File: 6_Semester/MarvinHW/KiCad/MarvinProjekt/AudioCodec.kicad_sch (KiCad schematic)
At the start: 0 parts

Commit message: made SD-Card, Audio Codec and Amplifier schematic
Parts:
- added C10, C11, C12, C13, C14, C15, C16, C17, C18, C19, C20, C21, C22, C23, C24, C25, C26, C27, C28, C29, C30, C31, C32, C5, C6, C7, C8, C9: C, symbol Device:C
- added FB1: Ferrite_Bead_Small, Inductor_SMD:L_0805_2012Metric, symbol Device:FerriteBead_Small
- added LS1: Speaker, symbol Device:Speaker
- added R10, R11, R12, R13, R14, R15, R16, R17, R18, R19, R20, R21, R22, R23, R24, R25, R26, R4, R5, R6, R7, R8, R9: R, symbol Device:R
- added U2: ~, Package_DFN_QFN:QFN-28-1EP_4x4mm_P0.4mm_EP2.3x2.3mm, symbol Library:ES8388
- added U3: ~, symbol Library:NS4150
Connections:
- new net: R22.2, R24.1, U3.2 (INP)
- new net: R14.1, U2.7
- new net: C23.1, C24.1, C25.1, FB1.2, U3.1 (VIN), U3.10 (PVIN)
- new net: R12.1, U2.1
- new net: C15.1, C18.1, U2.10
- new net: C20.2, U2.11
- new net: C19.2, U2.12
- new net: C7.1, C9.1, R6.2, U2.17
- new net: C14.1, C17.1, U2.19
- new net: C5.1, R4.1, R5.1, U2.2, U2.3
- new net: C13.1, C16.1, U2.20
- new net: C11.1, R9.1, U2.27
- new net: C12.1, R8.1, U2.28
- new net: R13.1, U2.5
- new net: R15.1, U2.6
- new net: R16.1, U2.8
- new net: C30.1, C32.1, LS1.1, R25.1
- new net: C28.1, C29.1
- new net: C19.1, R19.2
- new net: C26.1, C27.2, R22.1
- new net: C22.1, R21.1
- new net: C20.1, R20.2
- new net: R23.2, U3.3 (INN)
- new net: C31.2, C32.2, LS1.2, R26.1
- new net: C28.2, R23.1
- new net +3V3: C10.1, C6.1, C8.1, FB1.1, R10.1, R11.1, R17.1, R5.2, R6.1, R7.1, R7.2, U2.16
- new net ASDOUT: R16.2
- new net AUDIO_LS: C27.1, R21.2
- new net AUDIO_RL: C21.1, C22.2
- new net Audio_RL: R19.1, R20.1
- new net CE: R17.2, R18.1, U2.26
- new net DSDIN: R15.2
- new net GND: C10.2, C11.2, C12.2, C13.2, C14.2, C15.2, C16.2, C17.2, C18.2, C21.2, C23.2, C24.2, C25.2, C26.2, C29.2, C30.2, C31.1, C5.2, C6.2, C7.2, C8.2, C9.2, R18.2, R24.2, R4.2, U2.13, U2.18, U2.29, U2.4, U3.11 (GNDPAD), U3.4 (DGND), U3.6 (CLK), U3.7 (PGND)
- new net LRCK: R14.2
- new net LS+: R25.2, U3.8 (OUTP)
- new net LS-: R26.2, U3.9 (OUTN)
- new net LS_ENABLE: U3.5 (!SHDN)
- new net MCLK: R12.2
- new net SCL: R10.2, R8.2
- new net SCLK: R13.2
- new net SDA: R11.2, R9.2
- no-connect marks 0 -> 8
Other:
- note added: "AudioCodec schaltung Verstärker schaltung"
- note added: "Components near IC pins on the same layer, NO VIAS!"

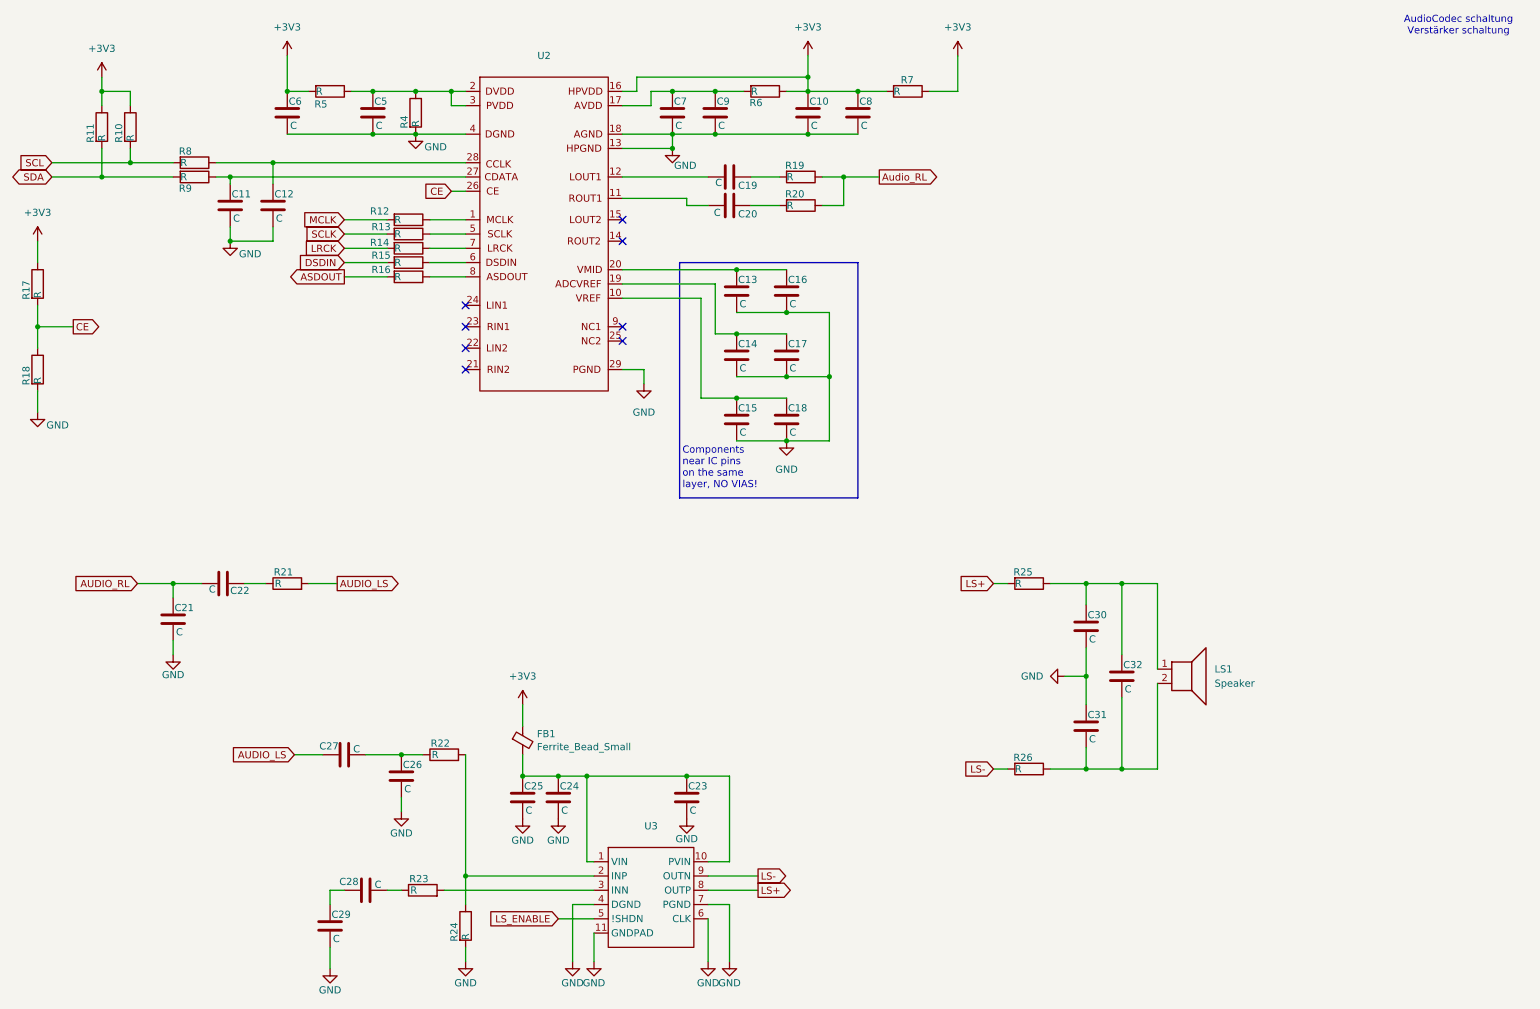
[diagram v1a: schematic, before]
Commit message: added datasheets and worked on schematic
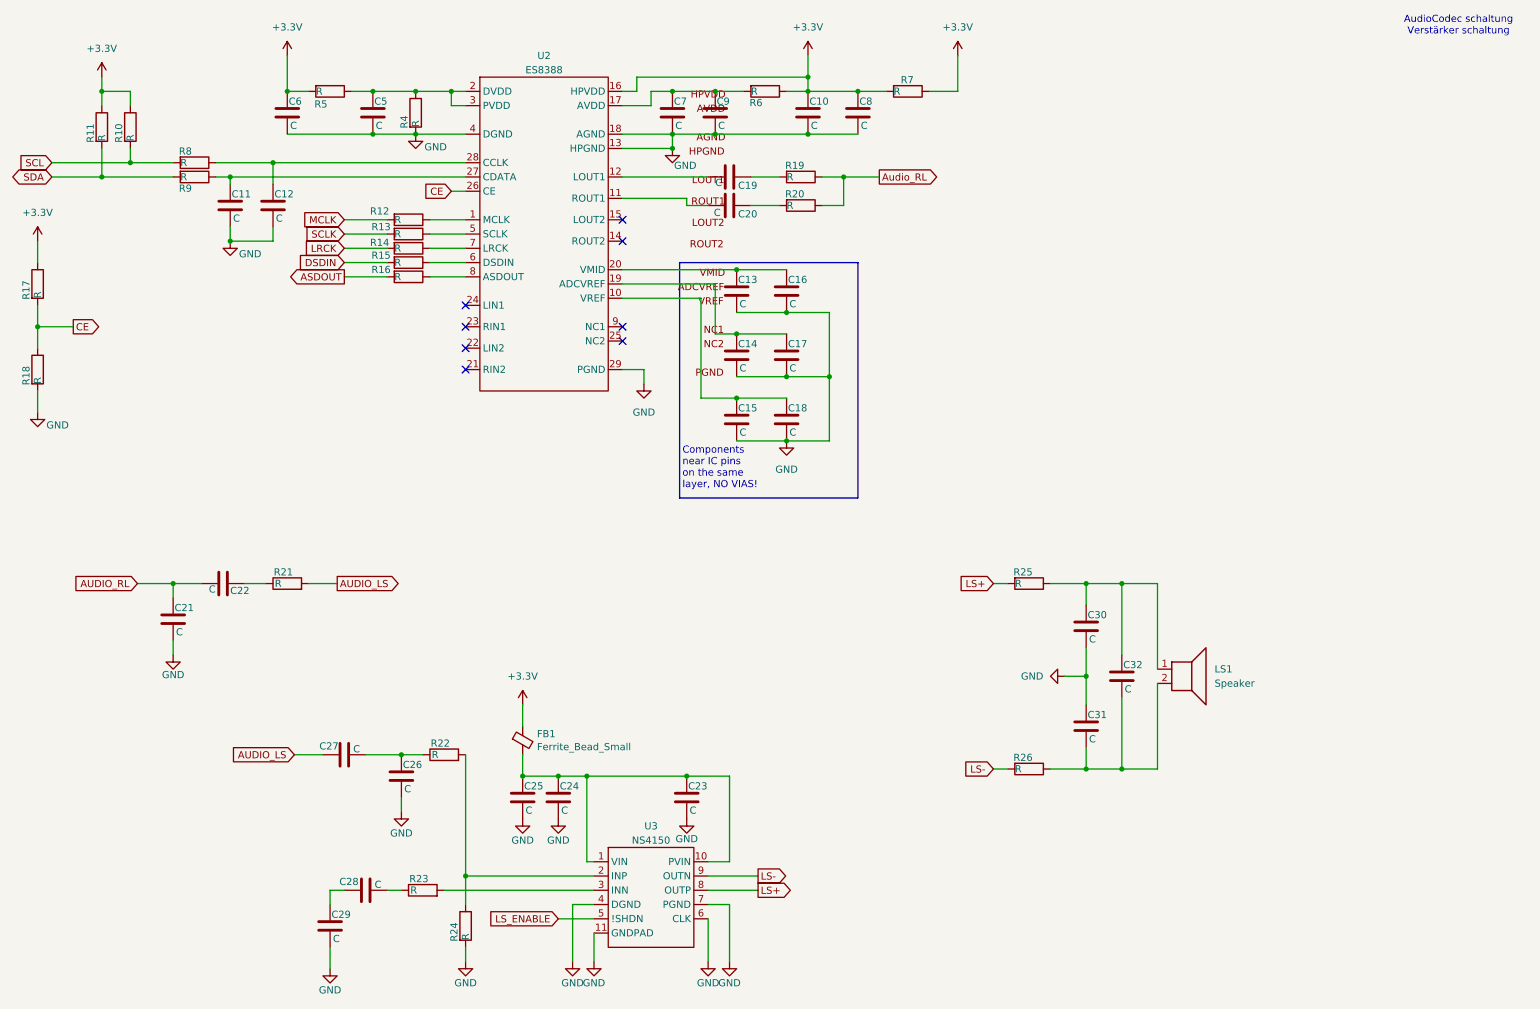
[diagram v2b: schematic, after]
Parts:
- U2: value ~ -> ES8388
- U3: value ~ -> NS4150
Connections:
- net +3V3 renamed +3.3V

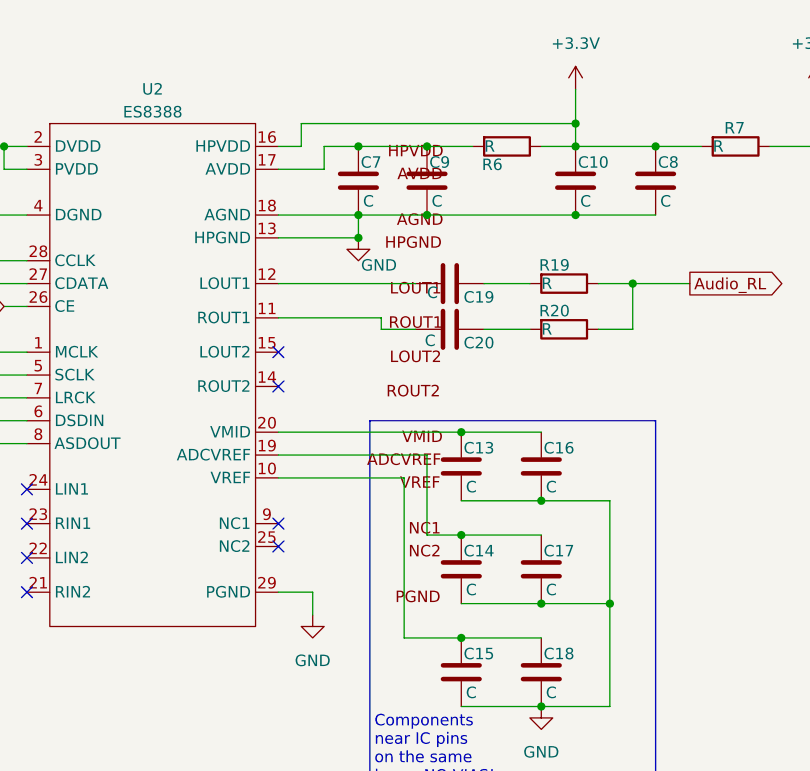
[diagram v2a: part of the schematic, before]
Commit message: renamed untitledsheet to crontrol
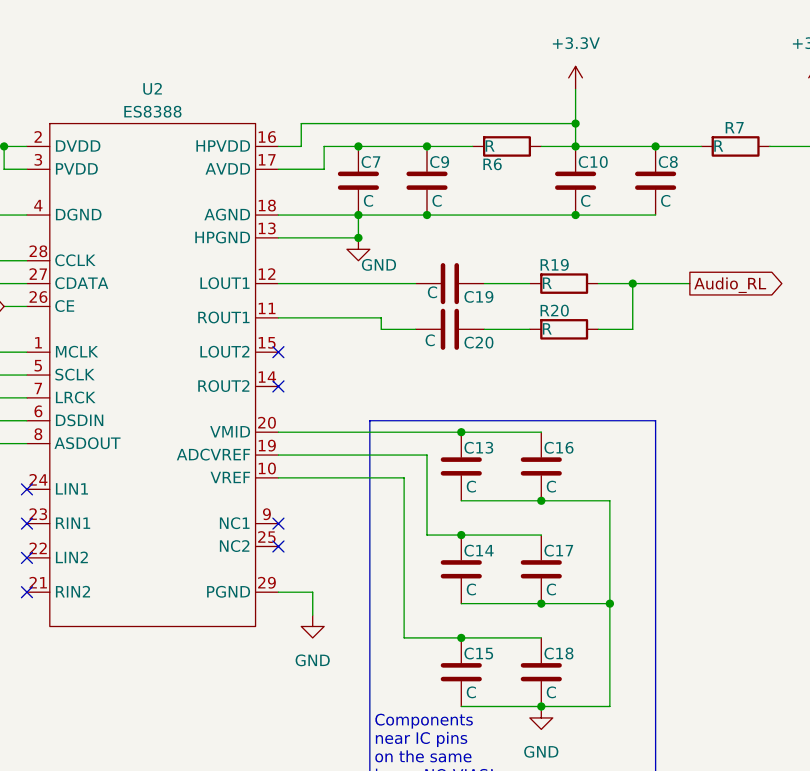
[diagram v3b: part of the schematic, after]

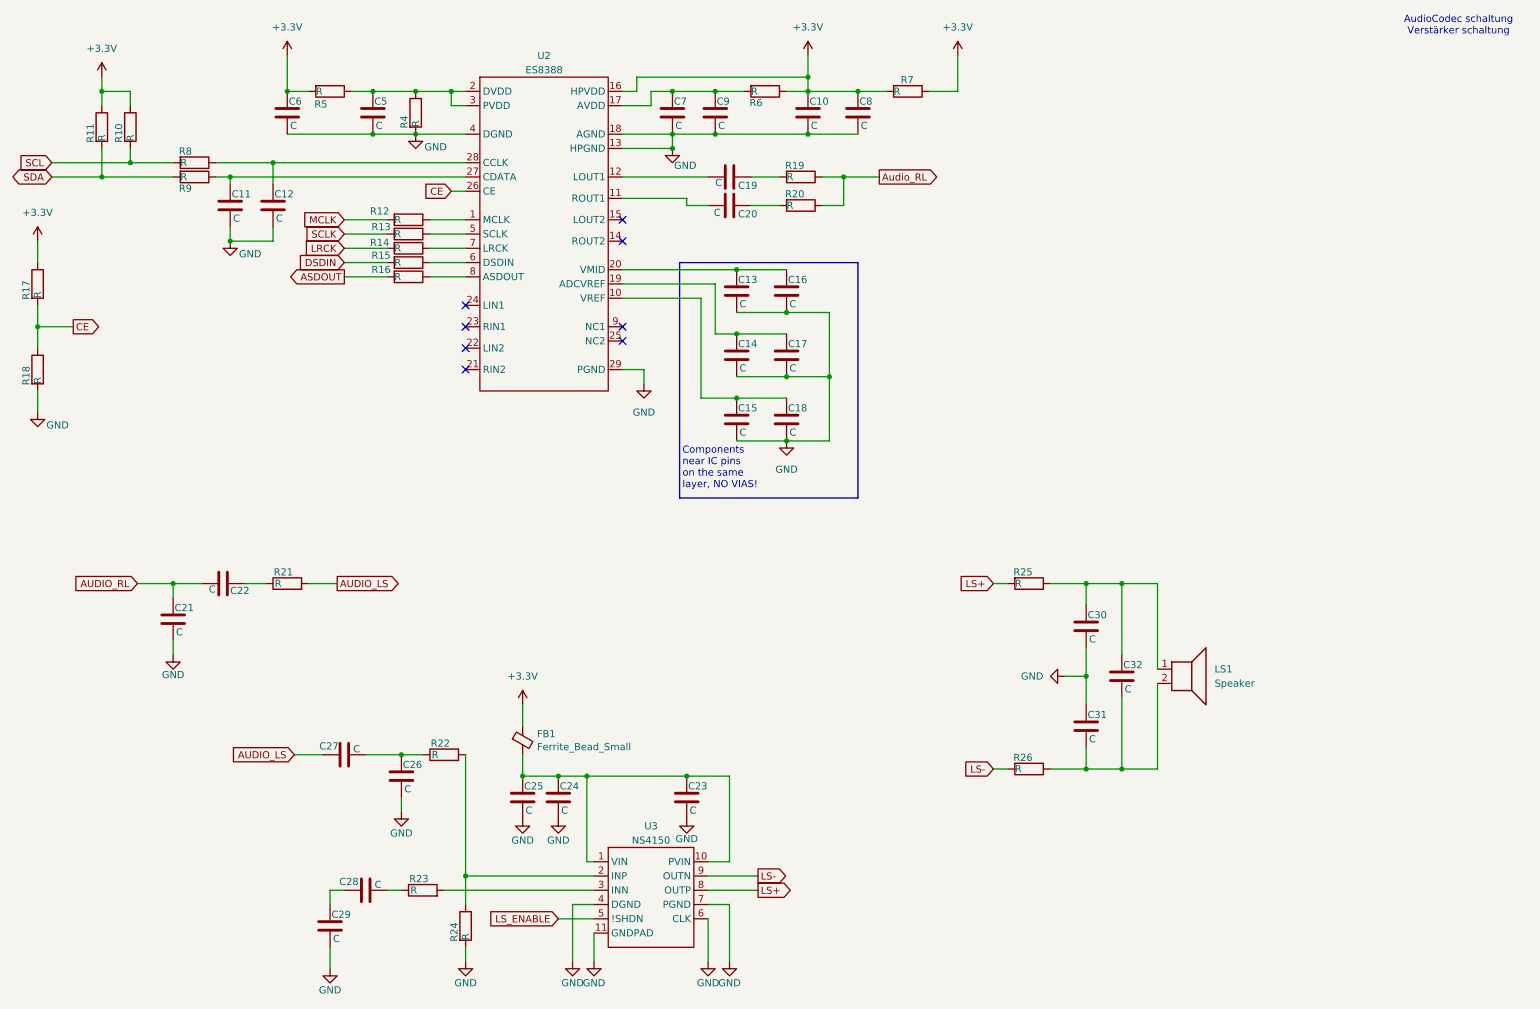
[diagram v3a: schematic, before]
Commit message: finished schematic working on footprints
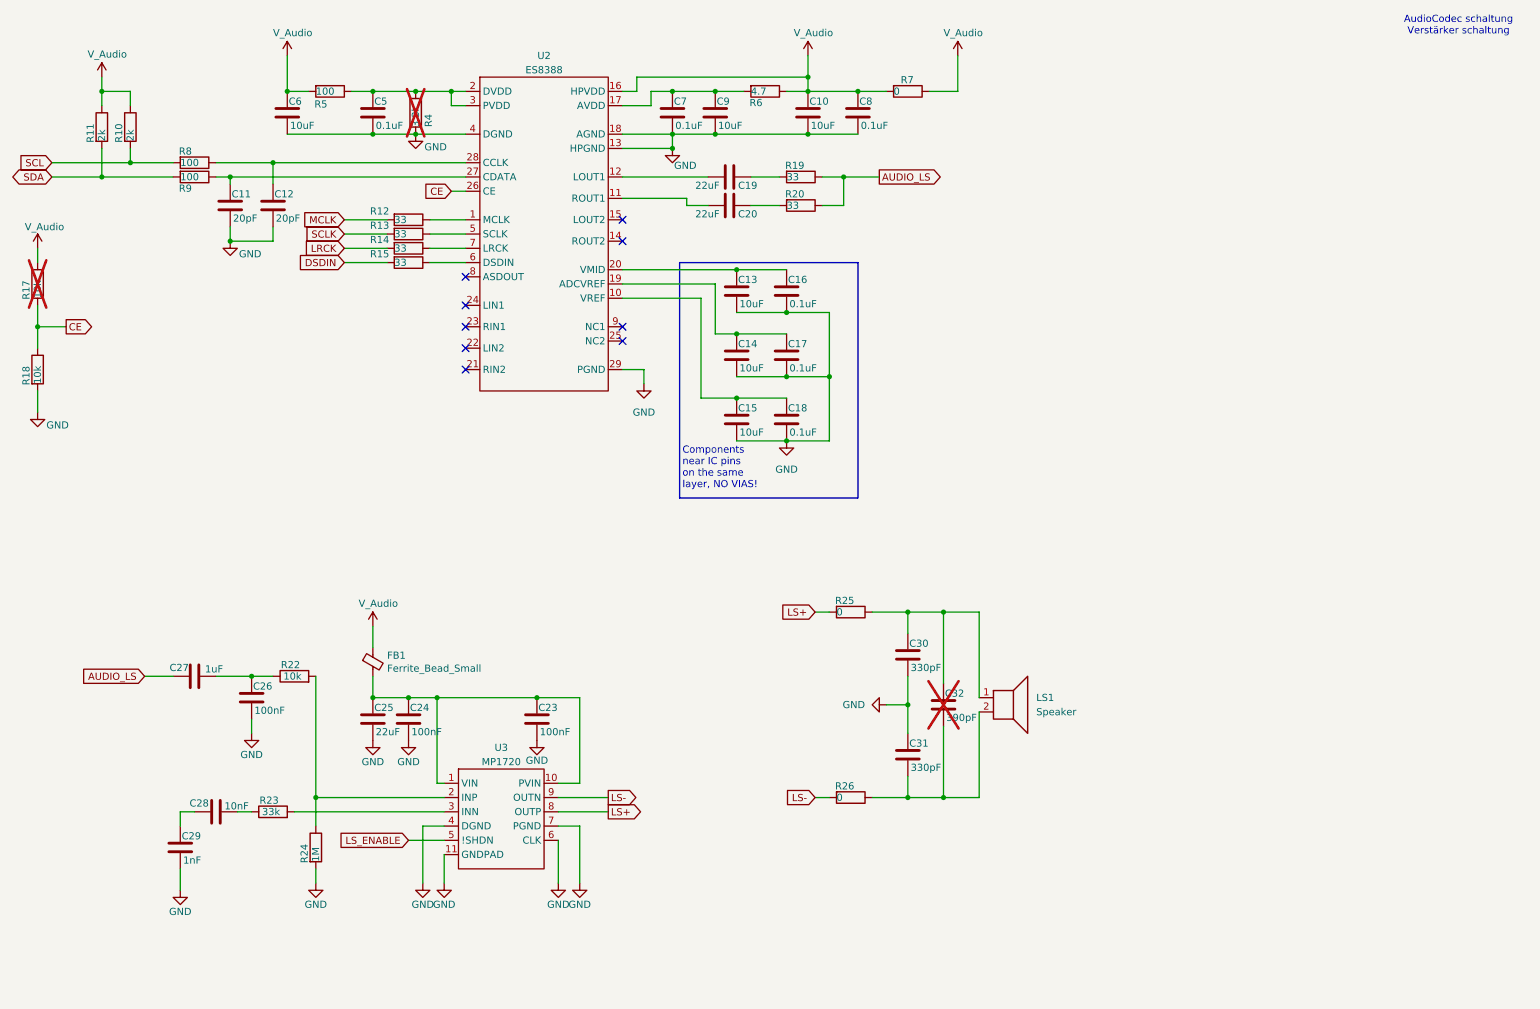
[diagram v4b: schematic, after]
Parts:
- removed C21, C22: C, symbol Device:C
- removed R16, R21: R, symbol Device:R
- C10, C13, C14, C15, C6, C9: value C -> 10uF; footprint (none) -> Capacitor_SMD:C_1206_3216Metric_Pad1.33x1.80mm_HandSolder
- C11, C12: value C -> 20pF; footprint (none) -> Capacitor_SMD:C_0805_2012Metric_Pad1.18x1.45mm_HandSolder
- C16, C17, C18, C5, C7, C8: value C -> 0.1uF; footprint (none) -> Capacitor_SMD:C_0805_2012Metric_Pad1.18x1.45mm_HandSolder
- C19, C20, C25: value C -> 22uF; footprint (none) -> Capacitor_SMD:C_0805_2012Metric_Pad1.18x1.45mm_HandSolder
- C23, C24, C26: value C -> 100nF; footprint (none) -> Capacitor_SMD:C_0805_2012Metric_Pad1.18x1.45mm_HandSolder
- C27: value C -> 1uF; footprint (none) -> Capacitor_SMD:C_0805_2012Metric_Pad1.18x1.45mm_HandSolder
- C28: value C -> 10nF; footprint (none) -> Capacitor_SMD:C_0805_2012Metric_Pad1.18x1.45mm_HandSolder
- C29: value C -> 1nF; footprint (none) -> Capacitor_SMD:C_0805_2012Metric_Pad1.18x1.45mm_HandSolder
- C30, C31: value C -> 330pF; footprint (none) -> Capacitor_SMD:C_0805_2012Metric_Pad1.18x1.45mm_HandSolder
- C32: value C -> 390pF; footprint (none) -> Capacitor_SMD:C_0805_2012Metric_Pad1.18x1.45mm_HandSolder; now not fitted
- R10, R11: value R -> 2k; footprint (none) -> Resistor_SMD:R_0805_2012Metric_Pad1.20x1.40mm_HandSolder
- R12, R13, R14, R15, R19, R20: value R -> 33; footprint (none) -> Resistor_SMD:R_0805_2012Metric_Pad1.20x1.40mm_HandSolder
- R17: value R -> 10k; footprint (none) -> Resistor_SMD:R_0805_2012Metric_Pad1.20x1.40mm_HandSolder; now not fitted
- R18, R22: value R -> 10k; footprint (none) -> Resistor_SMD:R_0805_2012Metric_Pad1.20x1.40mm_HandSolder
- R23: value R -> 33k; footprint (none) -> Resistor_SMD:R_0805_2012Metric_Pad1.20x1.40mm_HandSolder
- R24: value R -> 1M; footprint (none) -> Resistor_SMD:R_0805_2012Metric_Pad1.20x1.40mm_HandSolder
- R25, R26, R7: value R -> 0; footprint (none) -> Resistor_SMD:R_0805_2012Metric_Pad1.20x1.40mm_HandSolder
- R4: value R -> 3.3k; footprint (none) -> Resistor_SMD:R_0805_2012Metric_Pad1.20x1.40mm_HandSolder; now not fitted
- R5, R8, R9: value R -> 100; footprint (none) -> Resistor_SMD:R_0805_2012Metric_Pad1.20x1.40mm_HandSolder
- R6: value R -> 4.7; footprint (none) -> Resistor_SMD:R_0805_2012Metric_Pad1.20x1.40mm_HandSolder
- U3: value NS4150 -> MP1720
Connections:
- net Audio_RL is gone; now on net AUDIO_LS: R19.1, R20.1
- net +3.3V renamed V_Audio
- no-connect marks 8 -> 9
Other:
- moved on the sheet: C23, C24, C25, C26, C27, C28, C29, C30, C31, FB1, LS1, R22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

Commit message: finished all footprints and put the objects in place
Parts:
- LS1: footprint (none) -> Library:LS
- U3: footprint (none) -> Library:MP1720
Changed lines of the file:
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@@
 			)
 		)
-		(property "Footprint" ""
+		(property "Footprint" "Library:MP1720"
 			(at 102.87 153.67 0)
 			(effects
@@
 			)
 		)
-		(property "Footprint" ""
+		(property "Footprint" "Library:LS"
 			(at 193.04 139.7 0)
 			(effects

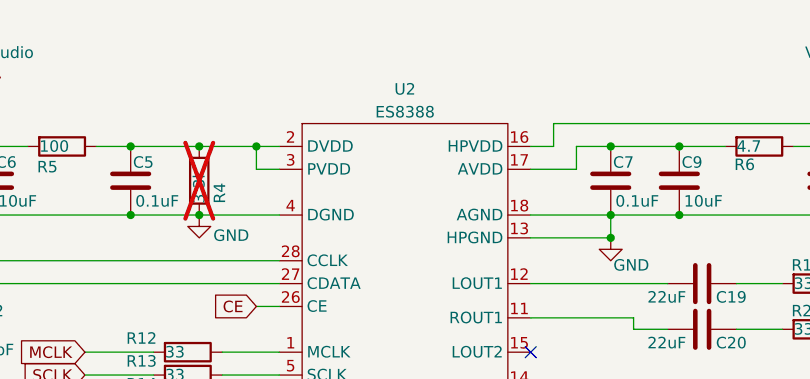
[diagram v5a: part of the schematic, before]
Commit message: add comonents to BoM
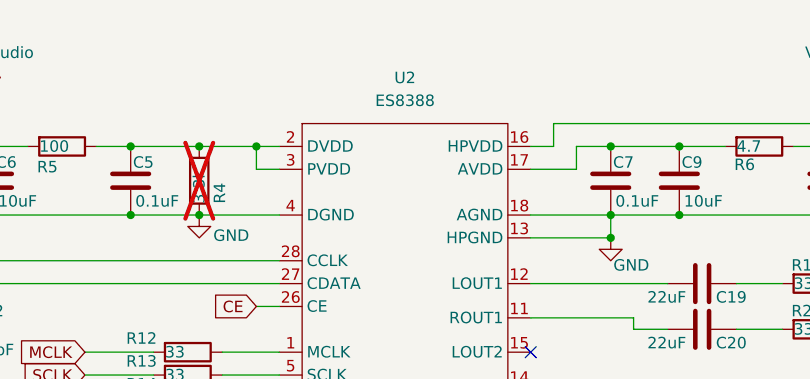
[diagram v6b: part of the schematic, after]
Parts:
- FB1: OrderNow (none) -> x; digikey (none) -> 732-1613-1-ND
- U2: LCSC Part (none) -> C365736; OrderNow (none) -> x

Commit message: finish evaluat components
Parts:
- R5, R8, R9: now not fitted
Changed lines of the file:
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@@
 		(in_bom yes)
 		(on_board yes)
-		(dnp no)
+		(dnp yes)
 		(property "Reference" "R9"
 			(at 45.466 43.942 90)
@@
 		(in_bom yes)
 		(on_board yes)
-		(dnp no)
+		(dnp yes)
 		(property "Reference" "R8"
 			(at 45.466 37.338 90)
@@
 		(in_bom yes)
 		(on_board yes)
-		(dnp no)
+		(dnp yes)
 		(property "Reference" "R5"
 			(at 69.596 28.956 90)
